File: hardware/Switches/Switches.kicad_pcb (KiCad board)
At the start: 2 copper layers, 120 x 75 mm, 173 parts, among them J101 BusBar, J102 BusBar, J103 BusBar, J104 BusBar, J105 Conn_02x03_Odd_Even, Q101 IPT015N10N5, Q102 IPT015N10N5, Q103 IPT015N10N5, Q104 IPT015N10N5, Q105 IPT015N10N5, Q106 IPT015N10N5, Q107 IPT015N10N5, Q108 IPT015N10N5, Q109 IPT015N10N5, Q110 IPT015N10N5, Q111 IPT015N10N5, Q112 IPT015N10N5, U101 UCC27211DDAR, U102 UCC27211DDAR

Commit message: wip: PCB updated
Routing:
- net /SL2_sen: track 17.4 -> 15.9 mm
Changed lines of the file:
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@@
     (thickness 1)
     (drawings 18)
-    (tracks 636)
+    (tracks 637)
     (zones 0)
     (modules 173)
@@
   (segment (start 154.75 95.45) (end 154.75 90.950048) (width 0.6) (layer F.Cu) (net 20))
   (segment (start 154.6125 92.6875) (end 154.6125 99.5125) (width 2) (layer F.Cu) (net 20))
-  (segment (start 170.3 95.480004) (end 163.854948 89.034952) (width 0.6) (layer B.Cu) (net 20))
+  (segment (start 158.500048 91) (end 156.535 89.034952) (width 0.6) (layer B.Cu) (net 20))
+  (segment (start 165.819996 91) (end 158.500048 91) (width 0.6) (layer B.Cu) (net 20))
+  (segment (start 170.3 95.480004) (end 165.819996 91) (width 0.6) (layer B.Cu) (net 20))
   (segment (start 170.3 108.05) (end 170.3 95.480004) (width 0.6) (layer B.Cu) (net 20))
   (segment (start 171.35 109.1) (end 170.3 108.05) (width 0.6) (layer B.Cu) (net 20))
-  (segment (start 163.854948 89.034952) (end 156.535 89.034952) (width 0.6) (layer B.Cu) (net 20))
   (segment (start 153.5125 107.9125) (end 154.4 108.8) (width 0.8) (layer F.Cu) (net 21))
   (segment (start 152.4 107.9125) (end 153.5125 107.9125) (width 0.8) (layer F.Cu) (net 21))
@@
   (via (at 169.9 86.1) (size 0.8) (drill 0.3) (layers F.Cu B.Cu) (net 34))
   (segment (start 169.9 87.3) (end 169.9 86.1) (width 0.3) (layer F.Cu) (net 34))
-  (segment (start 169.9 86.1) (end 164.9 86.1) (width 0.3) (layer B.Cu) (net 34))
   (via (at 162.8 81.1) (size 0.8) (drill 0.3) (layers F.Cu B.Cu) (net 34))
-  (segment (start 162.8 84) (end 162.8 81.1) (width 0.3) (layer B.Cu) (net 34))
-  (segment (start 164.9 86.1) (end 162.8 84) (width 0.3) (layer B.Cu) (net 34))
   (segment (start 162.8 83.015) (end 162.885 83.1) (width 0.3) (layer F.Cu) (net 34))
   (segment (start 162.8 81.1) (end 162.8 83.015) (width 0.3) (layer F.Cu) (net 34))
+  (segment (start 162.8 81.5) (end 162.8 81.1) (width 0.3) (layer B.Cu) (net 34))
+  (segment (start 167.4 86.1) (end 162.8 81.5) (width 0.3) (layer B.Cu) (net 34))
+  (segment (start 169.9 86.1) (end 167.4 86.1) (width 0.3) (layer B.Cu) (net 34))
   (segment (start 169.9 81.1125) (end 169.8875 81.1) (width 0.6) (layer F.Cu) (net 35))
   (segment (start 169.9 84.3) (end 169.9 81.1125) (width 0.6) (layer F.Cu) (net 35))

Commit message: Updating Switches PCB
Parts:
- removed C101, C104, C112, C113, C114, C115, C116, C117, C118, C119, C120 (x2), C121 (x2), C123, C124, C125, C126, C127, C128, C129, C130: 10u, Capacitor_SMD:C_1210_3225Metric_Pad1.33x2.70mm_HandSolder
- removed C135, C136, C137, C138, C139, C140, C141, C142, C143, C144, C145, C146, C147, C148, C149, C150, C151, C152, C153, C154: 100n, Capacitor_SMD:C_0805_2012Metric_Pad1.18x1.45mm_HandSolder
- removed C155, C156, C157, C158, C159, C160, C161, C162, C163, C164, C165, C166, C167, C168, C169, C170, C171, C172, C173, C174: 10n, Capacitor_SMD:C_0603_1608Metric_Pad1.08x0.95mm_HandSolder
- removed C175, C176, C177, C178, C179, C180, C181, C182, C183, C184, C185, C186, C187, C188, C189, C190, C191, C192, C193, C194: 1n, Capacitor_SMD:C_0603_1608Metric_Pad1.08x0.95mm_HandSolder
- R117: value 47k -> 5k6
- moved R117 5.07 mm to (167.2, 116.1)
- moved C134 1.53 mm to (169.8, 115.3), turned to 90 degrees
- moved TH101 0.94 mm to (171.8, 115.3), turned to 90 degrees
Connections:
- J105 pad 10: /SL1_sen -> GND
- J105 pad 11: /PWM_H1 -> /PWM_L1
- J105 pad 12: /SL2_sen -> /SL1_sen
- J105 pad 13: /PWM_L2 -> /PWM_H1
- J105 pad 14: /Vin_sen -> /SL2_sen
- J105 pad 15: /PWM_H2 -> /PWM_L2
- J105 pad 16: /TEMP1 -> /Vin_sen
- J105 pad 17: (no net) -> /PWM_H2
- J105 pad 18: GNDA -> /TEMP1
- J105 pad 19: (no net) -> +5VA
- J105 pad 5: (no net) -> +15V
- J105 pad 6: (no net) -> GND
- J105 pad 7: (no net) -> +15V
- J105 pad 8: (no net) -> GND
- J105 pad 9: /PWM_L1 -> +15V
- R117 pad 1: +15V -> +5VA
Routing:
- net GND: track 275.2 -> 377.1 mm, vias 14 -> 17
- net +5VA: track 0.00 -> 34.9 mm, vias 0 -> 2
- net +15V: track 77.2 -> 101.2 mm, vias 1 -> 2
- net /SL1_sen: track 16.1 -> 19.2 mm
- net /SL2_sen: track 15.9 -> 14.4 mm
- net /Vin_sen: track 11.7 -> 10.3 mm
- net Net-(R114-Pad2): track 75.1 -> 74.0 mm
- net /PWM_L2: track 16.5 -> 17.1 mm
- net /PWM_H1: track 18.8 -> 19.3 mm
- net /PWM_L1: track 17.0 -> 17.6 mm
- net /PWM_H2: track 14.8 -> 15.3 mm

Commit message: PCB updated, not yet finished
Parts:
- C131, C132, C133: value 1p -> 1n
- J101, J102: footprint Switches:BusBar -> Switches:BusBar1
- J103, J104: footprint Switches:BusBar -> Switches:BusBar2
- Q101, Q102, Q103, Q104, Q105, Q106, Q107, Q108, Q109, Q110, Q111, Q112: footprint Package_TO_SOT_SMD:Infineon_PG-HSOF-8-1_ThermalVias -> Switches:Infineon_PG-HSOF-8-1_ThermalVias_custom
- R122, R123: value 330 -> 3k3
- U101, U102: footprint Package_SO:SOIC-8-1EP_3.9x4.9mm_P1.27mm_EP2.514x3.2mm_ThermalVias -> Switches:SOIC-8-1EP_3.9x4.9mm_P1.27mm_EP2.514x3.2mm_ThermalVias
- moved J104 4.61 mm to (198.3, 100.5)
- moved J103 4.39 mm to (126.2, 100.5)
- moved J101 0.25 mm to (162.2, 128.3), turned to 180 degrees
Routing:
- net +BATT: track 112.1 -> 113.2 mm
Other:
- rule via_min_drill: 0.3 -> 0.2

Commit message: Done, not yet checked
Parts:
- removed C102, C105, C106: 100n, Capacitor_SMD:C_1210_3225Metric_Pad1.33x2.70mm_HandSolder
- removed R101, R109, R110: 10, Resistor_SMD:R_1210_3225Metric_Pad1.30x2.65mm_HandSolder
- added Csn101: 100n, Capacitor_SMD:C_1210_3225Metric_Pad1.33x2.70mm_HandSolder, F.Cu at (115.5, 90.6)
- added Csn102: NC, Capacitor_SMD:C_1210_3225Metric_Pad1.33x2.70mm_HandSolder, F.Cu at (112.3, 90.6)
- added Csn104: NC, Capacitor_SMD:C_1210_3225Metric_Pad1.33x2.70mm_HandSolder, F.Cu at (212.2, 90.6)
- added Csn105: 100n, Capacitor_SMD:C_1210_3225Metric_Pad1.33x2.70mm_HandSolder, F.Cu at (115.5, 119.1)
- added Csn106: NC, Capacitor_SMD:C_1210_3225Metric_Pad1.33x2.70mm_HandSolder, F.Cu at (112.2, 119.1)
- added Csn107: 100n, Capacitor_SMD:C_1210_3225Metric_Pad1.33x2.70mm_HandSolder, F.Cu at (212.2, 119.2)
- added Csn108: NC, Capacitor_SMD:C_1210_3225Metric_Pad1.33x2.70mm_HandSolder, F.Cu at (209.0, 119.2)
- added Dsn101: MBR2H100SFT3G, Diode_SMD:D_SOD-123F, F.Cu at (107.2, 85.5)
- added Dsn102: NC, Diode_SMD:D_SOD-123F, F.Cu at (109.5, 85.5)
- added Dsn103: MBR2H100SFT3G, Diode_SMD:D_SOD-123F, F.Cu at (215.1, 85.6)
- added Dsn104: NC, Diode_SMD:D_SOD-123F, F.Cu at (217.5, 85.6)
- added Dsn105: MBR2H100SFT3G, Diode_SMD:D_SOD-123F, F.Cu at (107.1, 114.2)
- added Dsn106: NC, Diode_SMD:D_SOD-123F, F.Cu at (109.5, 114.2)
- added Dsn107: MBR2H100SFT3G, Diode_SMD:D_SOD-123F, F.Cu at (215.1, 114.2)
- added Dsn108: NC, Diode_SMD:D_SOD-123F, F.Cu at (217.4, 114.2)
- added Rsn101: 10, Resistor_SMD:R_1210_3225Metric_Pad1.30x2.65mm_HandSolder, F.Cu at (115.5, 85.6)
- added Rsn102: NC, Resistor_SMD:R_1210_3225Metric_Pad1.30x2.65mm_HandSolder, F.Cu at (112.3, 85.6)
- added Rsn104: NC, Resistor_SMD:R_1210_3225Metric_Pad1.30x2.65mm_HandSolder, F.Cu at (212.2, 85.6)
- added Rsn105: 10, Resistor_SMD:R_1210_3225Metric_Pad1.30x2.65mm_HandSolder, F.Cu at (115.5, 114.0)
- added Rsn106: NC, Resistor_SMD:R_1210_3225Metric_Pad1.30x2.65mm_HandSolder, F.Cu at (112.3, 114.0)
- added Rsn107: 10, Resistor_SMD:R_1210_3225Metric_Pad1.30x2.65mm_HandSolder, F.Cu at (209.0, 114.2)
- added Rsn108: NC, Resistor_SMD:R_1210_3225Metric_Pad1.30x2.65mm_HandSolder, F.Cu at (212.2, 114.2)
- Q101, Q102, Q103, Q104, Q105, Q106, Q107, Q108, Q109, Q110, Q111, Q112: footprint Switches:Infineon_PG-HSOF-8-1_ThermalVias_custom -> Switches:Infineon_PG-HSOF-8-1_ThermalVias3
- moved Csn103 1.29 mm to (208.9, 90.6)
- moved Rsn103 1.25 mm to (208.9, 85.6)
- renumbered C103 to Csn103, R102 to Rsn103
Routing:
- net /SL1: track 106.9 -> 126.9 mm, vias 3 -> 527
- net GND: track 377.1 -> 360.8 mm, vias 17 -> 1105
- net +BATT: track 113.2 -> 104.7 mm, vias 0 -> 1088
- net /SL2: track 59.2 -> 50.9 mm, vias 3 -> 527
- net Net-(C106-Pad1): track 2.39 -> 0.00 mm
- net Net-(C105-Pad1): track 2.39 -> 0.00 mm
- net Net-(C102-Pad1): track 2.34 -> 0.00 mm
- net Net-(Csn103-Pad1): track 2.29 -> 0.00 mm
- net (no net): track 0.00 -> 1.21 mm
- net /GH1_1: track 14.6 -> 15.3 mm
- net Net-(R103-Pad2): track 66.5 -> 67.0 mm
- added copper zone on B.Cu, net +BATT
- added copper zone on B.Cu, net /SL1
- added copper zone on B.Cu, net /SL2
- added copper zone on B.Cu, net GND
- added copper zone on F.Cu, net Net-(Csn101-Pad1)
- added copper zone on F.Cu, net Net-(Csn103-Pad1)
- added copper zone on F.Cu, net Net-(Csn105-Pad1)
- added copper zone on F.Cu, net Net-(Csn107-Pad1)
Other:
- net class Default: clearance 0.3 -> 0.01
- rule trace_clearance: 0.3 -> 0.01

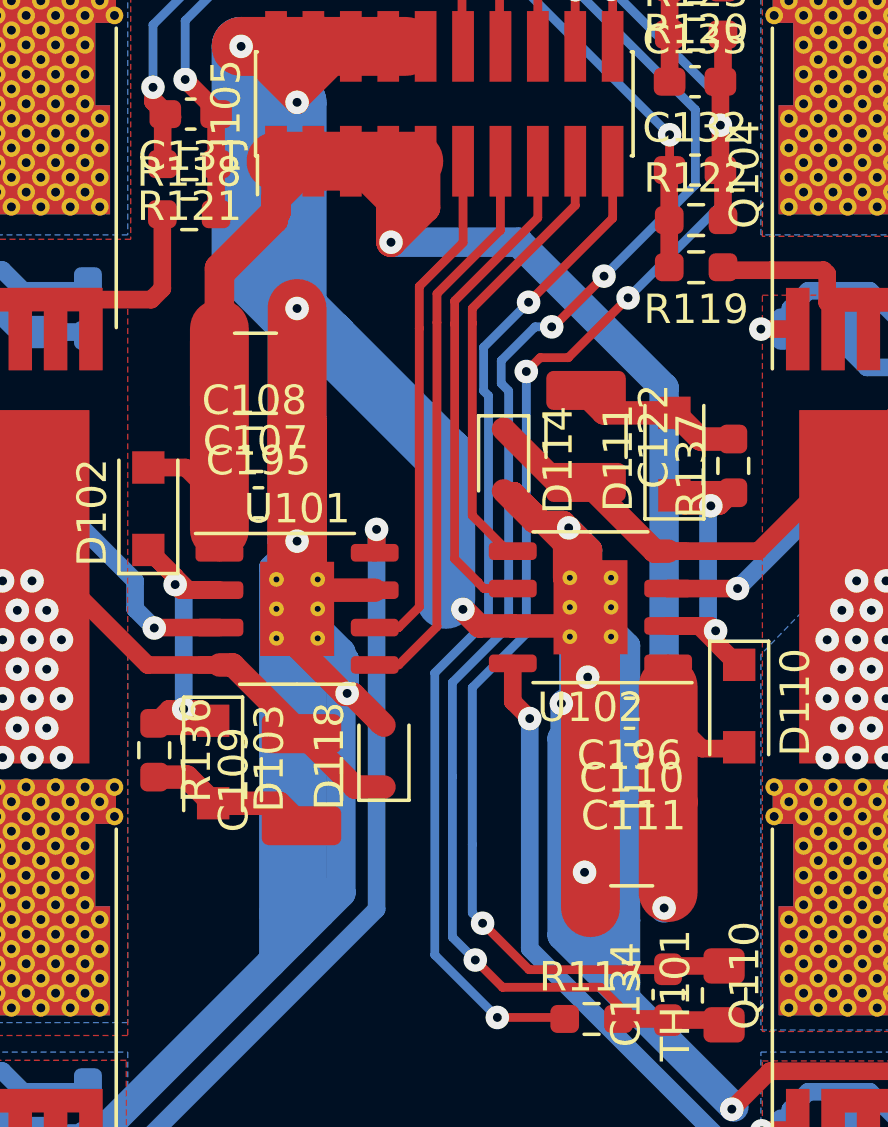
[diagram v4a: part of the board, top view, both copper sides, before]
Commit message: Changed to 4 layers because the need of tg-150 material. Gerbers added.
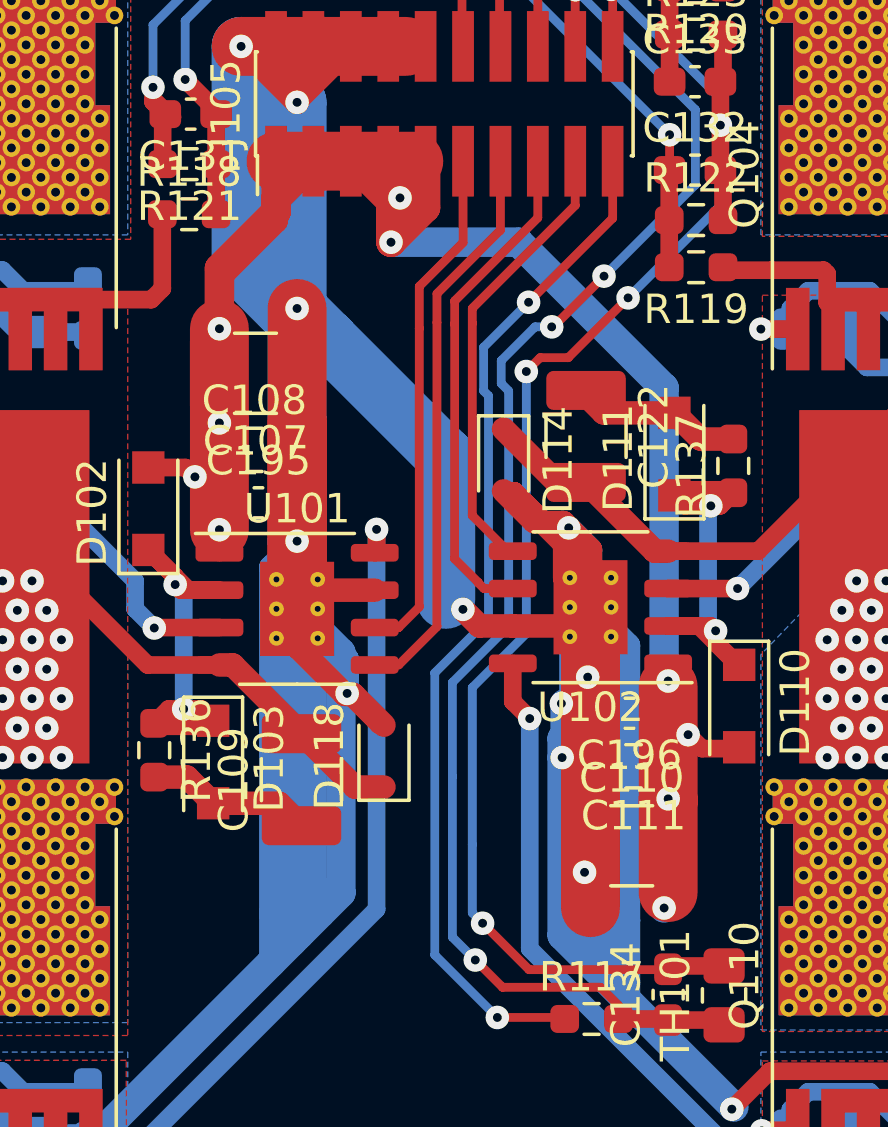
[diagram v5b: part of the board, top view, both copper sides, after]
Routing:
- net +15V: track 101.2 -> 102.2 mm, vias 2 -> 10
- net GND: vias 1105 -> 1106
- added copper zone on In2.Cu, net +15V
- added copper zone on In1.Cu, net +BATT
- added copper zone on In2.Cu, net +BATT
- added copper zone on In1.Cu, net /SL1
- added copper zone on In2.Cu, net /SL1
- added copper zone on In1.Cu, net /SL2
- added copper zone on In2.Cu, net /SL2
- added copper zone on In1.Cu, net GND
- added copper zone on In2.Cu, net GND
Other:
- copper layers 2 -> 4

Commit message: wip controle holes
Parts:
- added REF**: ControleHoles, Switches:ControleHoles, F.Cu at (162.8, 97.8)
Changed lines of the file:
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@@
   (general
     (thickness 1)
-    (drawings 23)
+    (drawings 24)
     (tracks 4009)
     (zones 0)
-    (modules 107)
+    (modules 108)
     (nets 40)
   )
   (page A4)
   (layers
-    (0 F.Cu mixed)
-    (1 In1.Cu mixed)
-    (2 In2.Cu mixed)
-    (31 B.Cu mixed)
-    (32 B.Adhes user)
-    (33 F.Adhes user)
-    (34 B.Paste user)
-    (35 F.Paste user)
-    (36 B.SilkS user)
-    (37 F.SilkS user)
-    (38 B.Mask user)
-    (39 F.Mask user)
+    (0 F.Cu mixed hide)
+    (1 In1.Cu mixed hide)
+    (2 In2.Cu mixed hide)
+    (31 B.Cu mixed hide)
+    (32 B.Adhes user hide)
+    (33 F.Adhes user hide)
+    (34 B.Paste user hide)
+    (35 F.Paste user hide)
+    (36 B.SilkS user hide)
+    (37 F.SilkS user hide)
+    (38 B.Mask user hide)
+    (39 F.Mask user hide)
     (40 Dwgs.User user)
     (41 Cmts.User user)
@@
     (add_net "Net-(R114-Pad2)")
   )
+  (module Switches:ControleHoles (layer F.Cu)
+    (at 162.75 97.85 90)
+    (fp_text reference REF** (at 0 0.5 90) (layer F.SilkS)
+      (effects (font (size 1 1) (thickness 0.15)))
+    )
+    (fp_text value ControleHoles (at 0 -0.5 90) (layer F.Fab)
+      (effects (font (size 1 1) (thickness 0.15)))
+    )
+    (pad "" np_thru_hole circle (at -32.37842 -12.99954 90) (size 3.200001 3.200001) (drill 3.200001) (layers *.Cu *.Mask))
+    (pad "" np_thru_hole circle (at 30.61758 -12.99954 90) (size 3.200001 3.200001) (drill 3.200001) (layers *.Cu *.Mask))
+    (pad "" np_thru_hole circle (at -32.37842 15.75046 90) (size 3.200001 3.200001) (drill 3.200001) (layers *.Cu *.Mask))
+    (pad "" np_thru_hole circle (at 30.61758 15.75046 90) (size 3.200001 3.200001) (drill 3.200001) (layers *.Cu *.Mask))
+    (pad "" thru_hole circle (at 12.79144 -0.49784 90) (size 1.524 1.524) (drill 0.0254) (layers *.Cu *.Mask))
+  )
   (module Switches:Infineon_PG-HSOF-8-1_ThermalVias3 locked (layer F.Cu)
     (at 201.8 114.65 90)
@@
     )
   )
+  (dimension 18.25 (width 0.15) (layer Dwgs.User)
+    (gr_text "18.250 mm" (at 167.5 75.925 90) (layer Dwgs.User)
+      (effects (font (size 1 1) (thickness 0.15)))
+    )
+    (feature1 (pts (xy 162.25 66.8) (xy 166.786421 66.8)))
+    (feature2 (pts (xy 162.25 85.05) (xy 166.786421 85.05)))
+    (crossbar (pts (xy 166.2 85.05) (xy 166.2 66.8)))
+    (arrow1a (pts (xy 166.2 66.8) (xy 166.786421 67.926504)))
+    (arrow1b (pts (xy 166.2 66.8) (xy 165.613579 67.926504)))
+    (arrow2a (pts (xy 166.2 85.05) (xy 166.786421 83.923496)))
+    (arrow2b (pts (xy 166.2 85.05) (xy 165.613579 83.923496)))
+  )
+  (dimension 68.5 (width 0.15) (layer Dwgs.User)
+    (gr_text "68.500 mm" (at 225.3 101.05 270) (layer Dwgs.User)
+      (effects (font (size 1 1) (thickness 0.15)))
+    )
+    (feature1 (pts (xy 222.25 135.3) (xy 224.586421 135.3)))
+    (feature2 (pts (xy 222.25 66.8) (xy 224.586421 66.8)))
+    (crossbar (pts (xy 224 66.8) (xy 224 135.3)))
+    (arrow1a (pts (xy 224 135.3) (xy 223.413579 134.173496)))
+    (arrow1b (pts (xy 224 135.3) (xy 224.586421 134.173496)))
+    (arrow2a (pts (xy 224 66.8) (xy 223.413579 67.926504)))
+    (arrow2b (pts (xy 224 66.8) (xy 224.586421 67.926504)))
+  )
   (dimension 59 (width 0.15) (layer Dwgs.User)
     (gr_text "59.000 mm" (at 93.501835 101.05 270) (layer Dwgs.User)
@@
     (arrow2b (pts (xy 92.445233 63.55) (xy 93.031654 64.676504)))
   )
-  (dimension 35 (width 0.15) (layer Dwgs.User)
-    (gr_text "35.000 mm" (at 201.25 56.35) (layer Dwgs.User)
-      (effects (font (size 1 1) (thickness 0.15)))
-    )
-    (feature1 (pts (xy 218.75 71.55) (xy 218.75 57.063579)))
-    (feature2 (pts (xy 183.75 71.55) (xy 183.75 57.063579)))
-    (crossbar (pts (xy 183.75 57.65) (xy 218.75 57.65)))
-    (arrow1a (pts (xy 218.75 57.65) (xy 217.623496 58.236421)))
-    (arrow1b (pts (xy 218.75 57.65) (xy 217.623496 57.063579)))
-    (arrow2a (pts (xy 183.75 57.65) (xy 184.876504 58.236421)))
-    (arrow2b (pts (xy 183.75 57.65) (xy 184.876504 57.063579)))
-  )
   (dimension 36 (width 0.15) (layer Dwgs.User)
     (gr_text "36.000 mm" (at 162.1 136.5) (layer Dwgs.User)
@@
   (gr_line (start 102.25 138.55) (end 222.25 63.55) (layer Dwgs.User) (width 0.15))
   (dimension 100 (width 0.15) (layer Dwgs.User)
-    (gr_text "100.000 mm" (at 233.8 101.05 270) (layer Dwgs.User)
+    (gr_text "100.000 mm" (at 230.75 101.05 270) (layer Dwgs.User)
       (effects (font (size 1 1) (thickness 0.15)))
     )
-    (feature1 (pts (xy 222.25 151.05) (xy 233.086421 151.05)))
-    (feature2 (pts (xy 222.25 51.05) (xy 233.086421 51.05)))
-    (crossbar (pts (xy 232.5 51.05) (xy 232.5 151.05)))
-    (arrow1a (pts (xy 232.5 151.05) (xy 231.913579 149.923496)))
-    (arrow1b (pts (xy 232.5 151.05) (xy 233.086421 149.923496)))
-    (arrow2a (pts (xy 232.5 51.05) (xy 231.913579 52.176504)))
-    (arrow2b (pts (xy 232.5 51.05) (xy 233.086421 52.176504)))
+    (feature1 (pts (xy 222.25 151.05) (xy 230.036421 151.05)))
+    (feature2 (pts (xy 222.25 51.05) (xy 230.036421 51.05)))
+    (crossbar (pts (xy 229.45 51.05) (xy 229.45 151.05)))
+    (arrow1a (pts (xy 229.45 151.05) (xy 228.863579 149.923496)))
+    (arrow1b (pts (xy 229.45 151.05) (xy 230.036421 149.923496)))
+    (arrow2a (pts (xy 229.45 51.05) (xy 228.863579 52.176504)))
+    (arrow2b (pts (xy 229.45 51.05) (xy 230.036421 52.176504)))
   )
   (dimension 120 (width 0.15) (layer Dwgs.User)
